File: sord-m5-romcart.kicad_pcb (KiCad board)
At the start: 2 copper layers, 99.3 x 62.5 mm, 8 parts, among them SW1 Choose ROM, U2 27C256, U3 74LS00

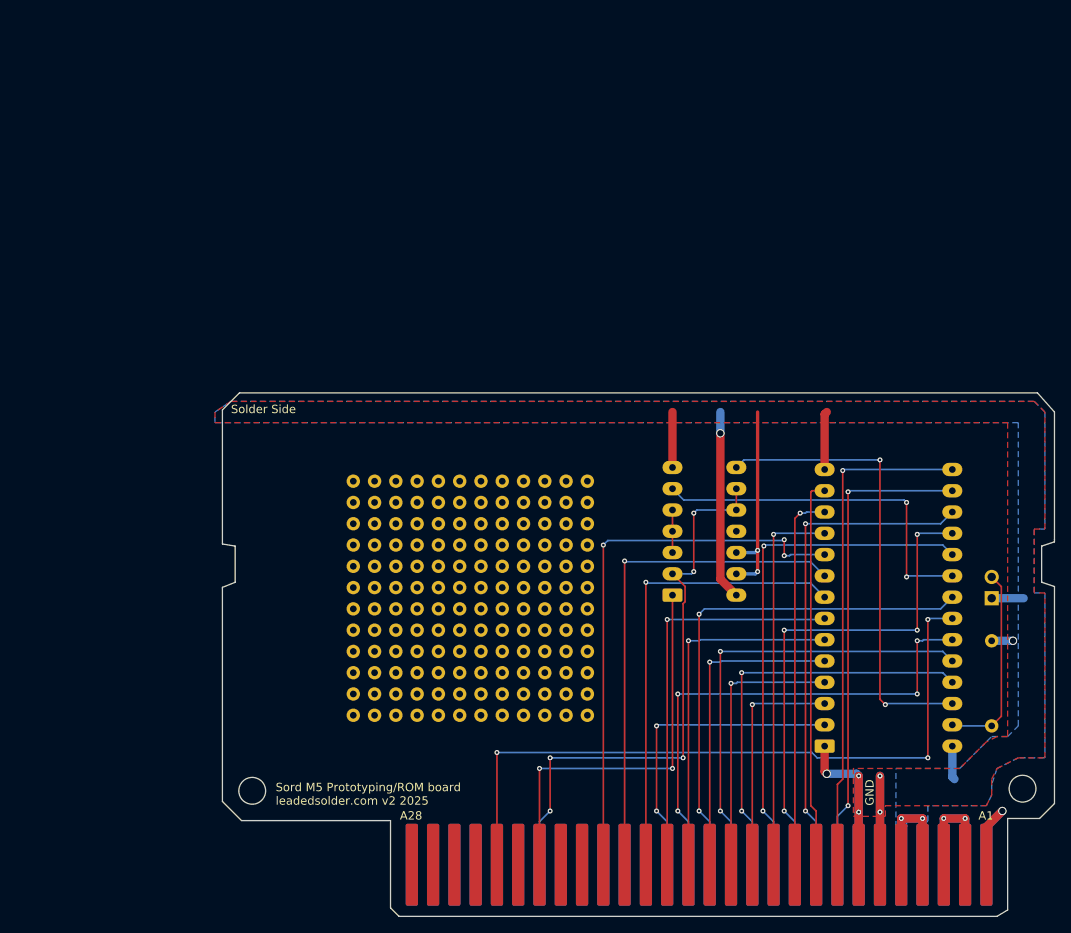
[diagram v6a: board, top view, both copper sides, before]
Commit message: Converted to ROM1 base, re-routed
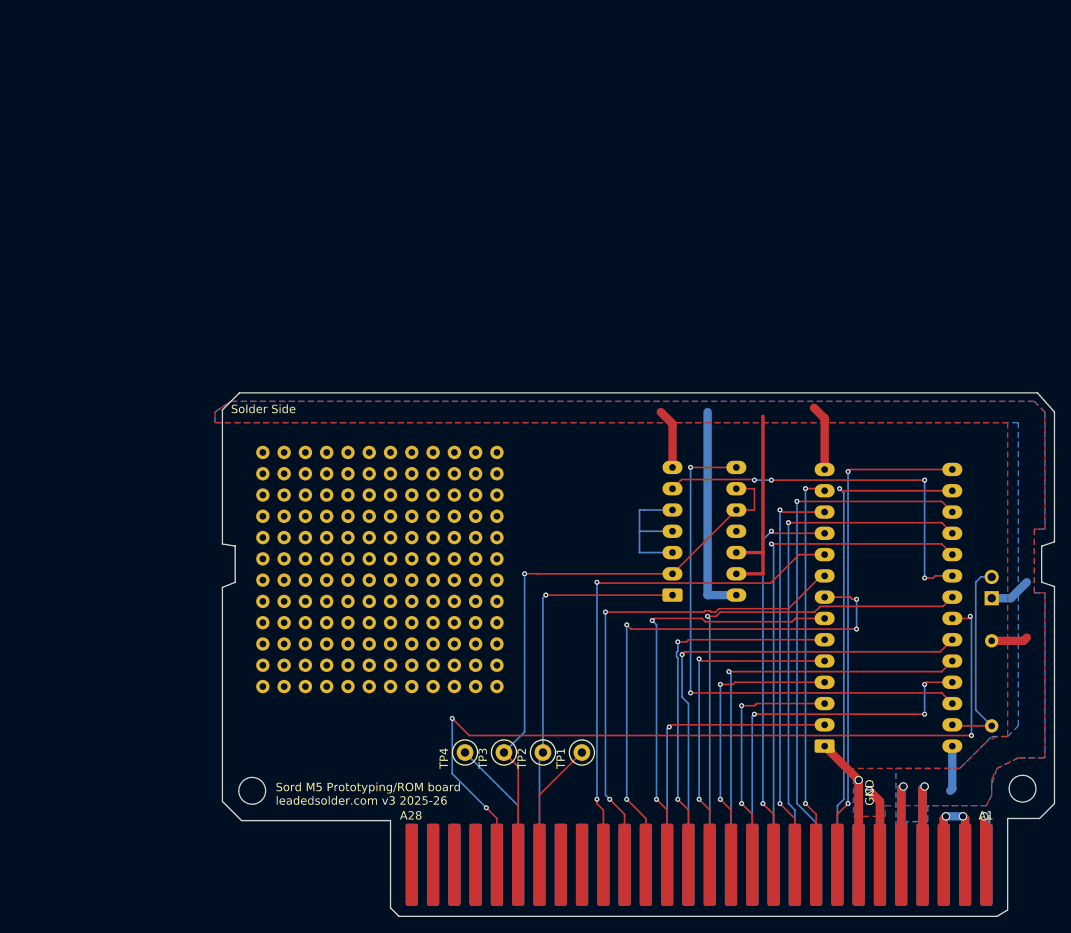
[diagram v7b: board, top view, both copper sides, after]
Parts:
- added TP1: TestPoint, TestPoint:TestPoint_Loop_D1.80mm_Drill1.0mm_Beaded, F.Cu at (143.5, 134.6)
- added TP2: TestPoint, TestPoint:TestPoint_Loop_D1.80mm_Drill1.0mm_Beaded, F.Cu at (138.8, 134.6)
- added TP3: TestPoint, TestPoint:TestPoint_Loop_D1.80mm_Drill1.0mm_Beaded, F.Cu at (134.2, 134.6)
- added TP4: TestPoint, TestPoint:TestPoint_Loop_D1.80mm_Drill1.0mm_Beaded, F.Cu at (129.5, 134.6)
- REF**: moved to F.Cu
- moved REF** 11.3 mm to (119.4, 112.8)
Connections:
- U1 pad B23: unconnected-(U1-~{EXM}-PadB23) -> /~{EXM}
- U3 pad 1: /~{ROM0} -> /~{ROM1}
- U3 pad 10: /~{ROM1} -> /~{ROM2}
- U3 pad 2: /~{ROM1} -> /~{ROM2}
- U3 pad 9: /~{ROM1} -> /~{ROM2}
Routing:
- net /~{ROM2}: track 0.00 -> 71.8 mm, vias 0 -> 1
- net /~{ROM0}: track 48.1 -> 15.5 mm, vias 2 -> 0
- net /~{ROM1}: track 69.2 -> 47.6 mm, vias 5 -> 1
- net /~{EXM}: track 0.00 -> 16.0 mm
- net +5V: track 57.7 -> 73.5 mm, vias 3 -> 2
- net /~{MEM_RD}: track 84.6 -> 99.0 mm, vias 3 -> 4
- net Net-(U3-Pad3): track 5.08 -> 16.9 mm
- net /ROM_A13: track 55.0 -> 64.2 mm
- net /A2: track 55.8 -> 64.7 mm, vias 1 -> 4
- net /A0: track 66.8 -> 62.7 mm, vias 3 -> 2
- net /D5: track 59.3 -> 63.4 mm, vias 2 -> 1
- net /A9: track 54.1 -> 50.4 mm, vias 2 -> 1
- net /A8: track 49.1 -> 45.4 mm, vias 2 -> 3
- net /A3: track 48.1 -> 50.9 mm, vias 1 -> 2
- net /~{ROM_CS}: track 43.0 -> 45.7 mm, vias 2 -> 4
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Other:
- board text added: "Sord M5 Prototyping/ROM board leadedsolder.com v3 2025-26"
- board text removed: "Sord M5 Prototyping/ROM board leadedsolder.com v2 2025"
